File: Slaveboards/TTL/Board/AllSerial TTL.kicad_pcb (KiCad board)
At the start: 2 copper layers, 67.4 x 44.8 mm, 3 parts, among them X1 ALLSERIALSLAVE, X2 AKL18X-10W, X3 PinHeader_2x03_P2.54mm_Horizo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

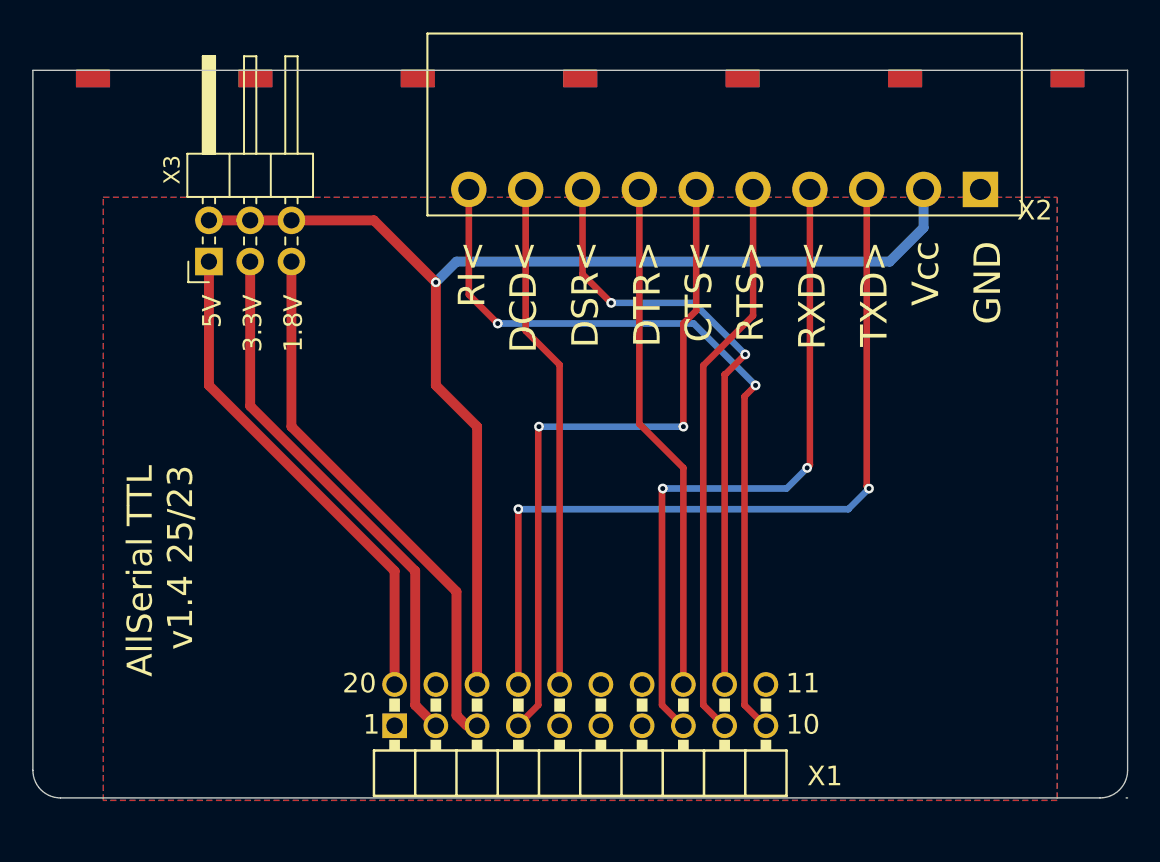
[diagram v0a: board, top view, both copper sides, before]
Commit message: Update AllSerial libraries
update projects
add slave project template
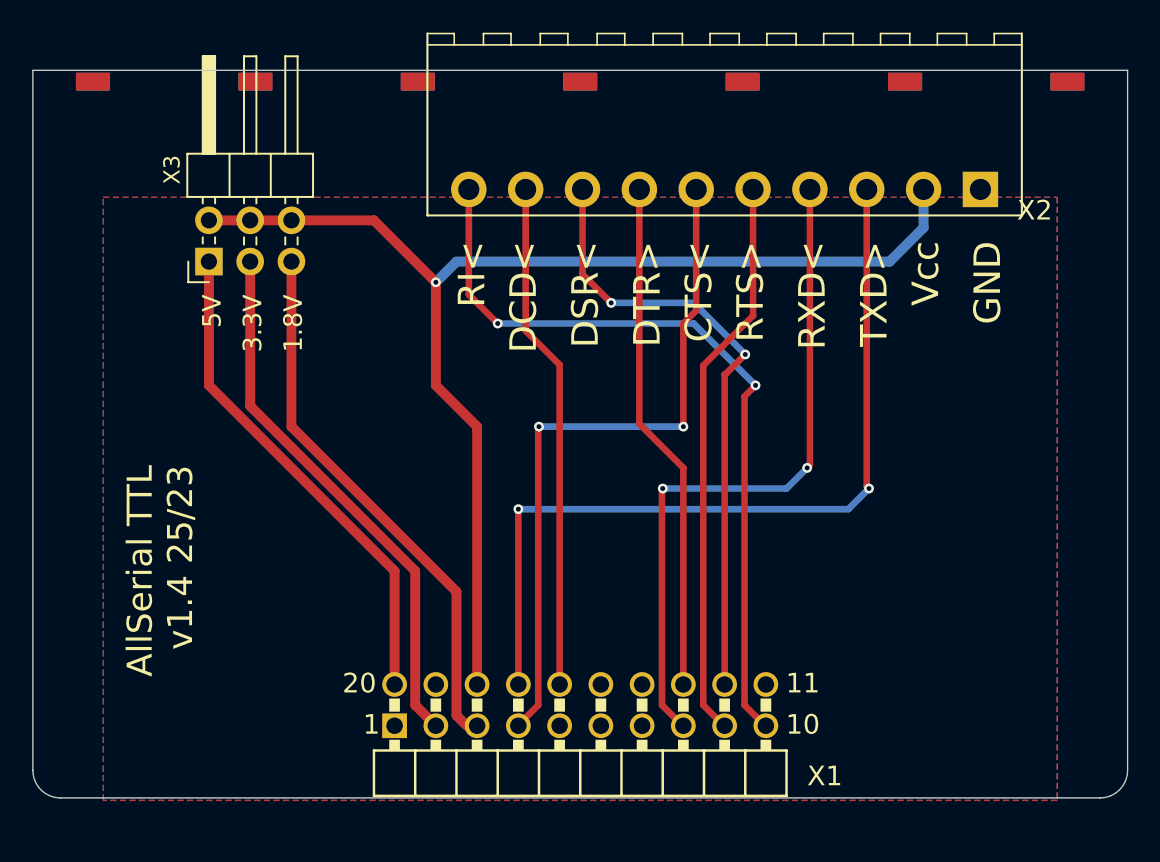
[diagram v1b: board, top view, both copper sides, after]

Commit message: Migrate to KiCad 9
Add eBus board
Add various libraries
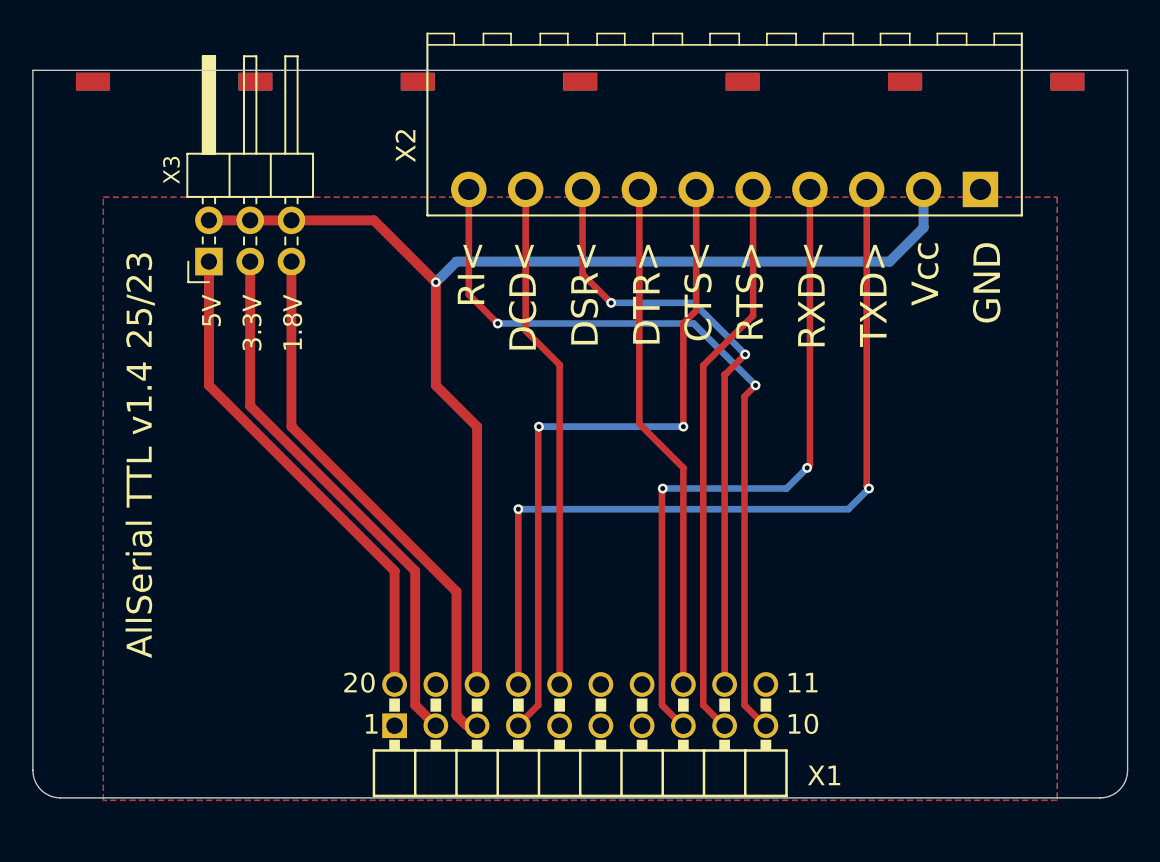
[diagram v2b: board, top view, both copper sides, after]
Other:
- board text added: "AllSerial TTL ${REVISION} ${ISSUE_DATE}"
- board text removed: "AllSerial TTL v1.4 25/23"
